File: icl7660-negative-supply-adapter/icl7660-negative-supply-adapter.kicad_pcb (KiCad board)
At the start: 2 copper layers, 33 x 45.7 mm, 11 parts, among them J1 Power Supply, J2 Eurorack_Power_Large, U1 ICL7660

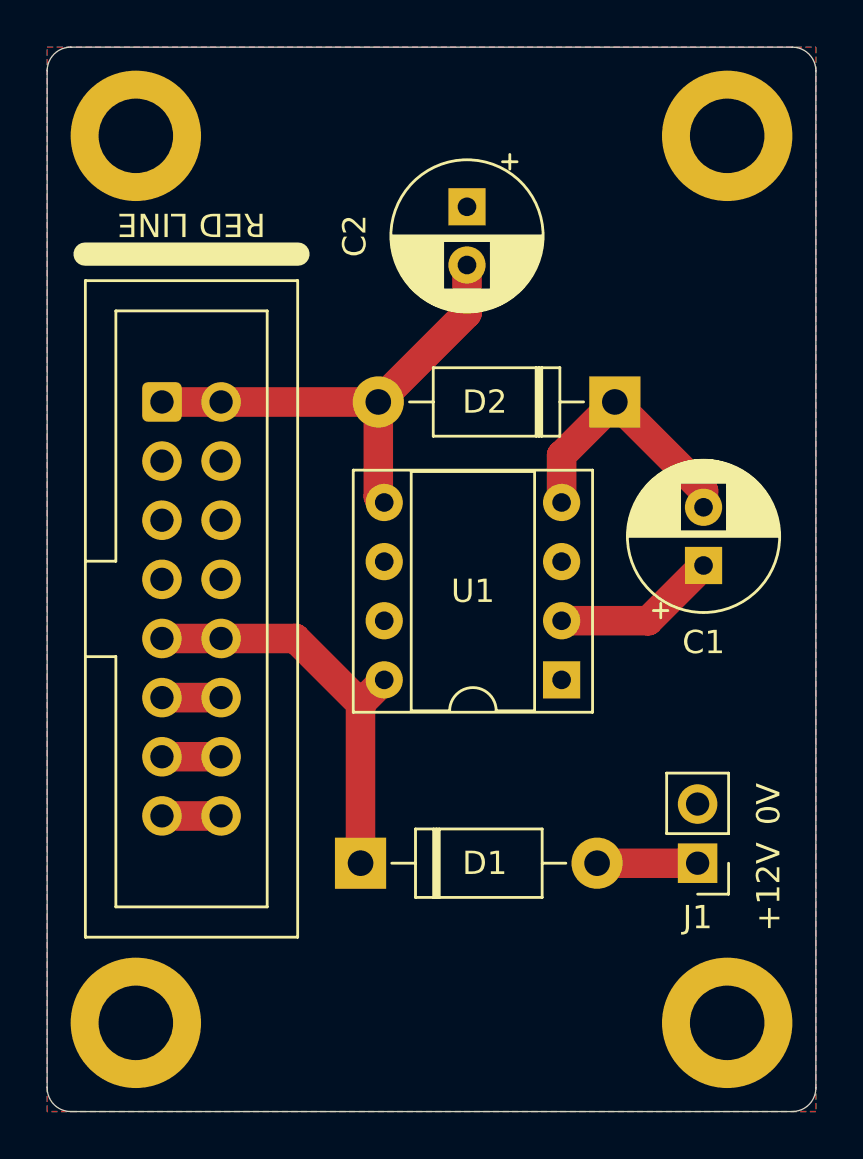
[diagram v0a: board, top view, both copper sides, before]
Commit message: update iclc7660 adapter with new footprints
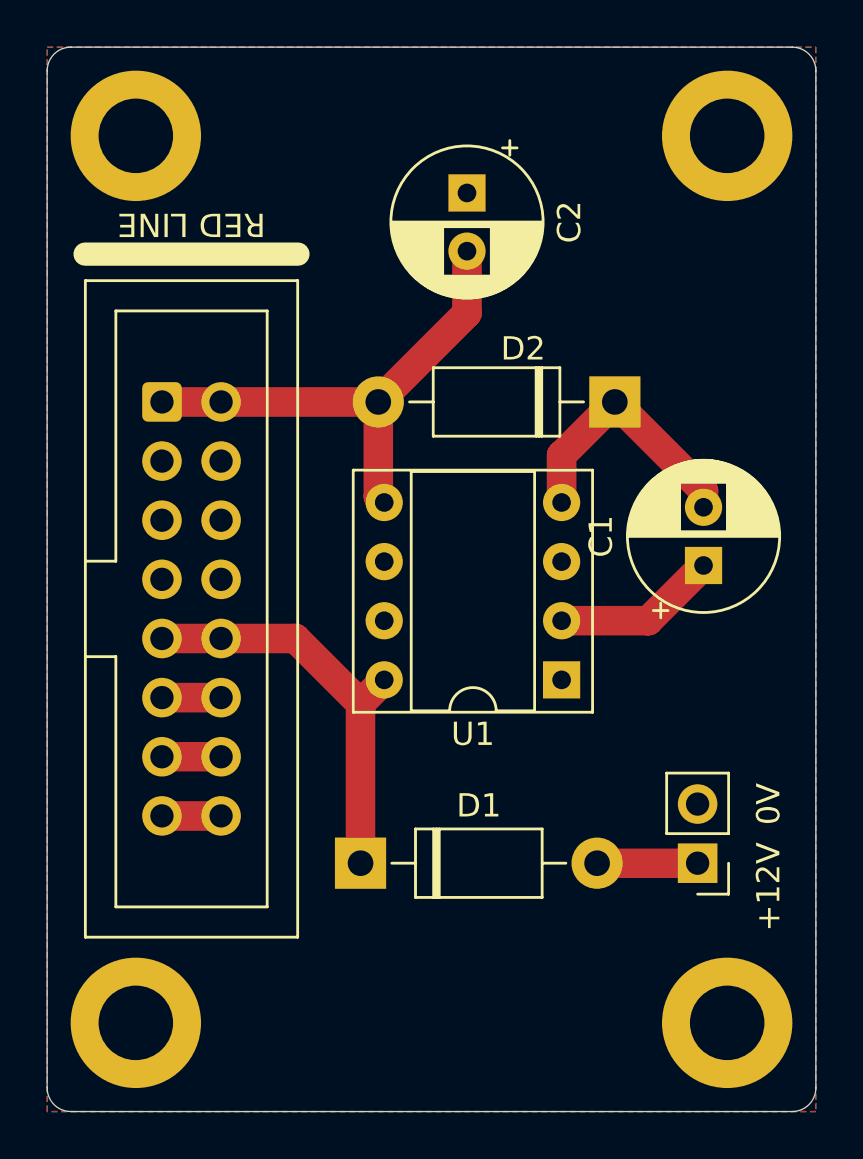
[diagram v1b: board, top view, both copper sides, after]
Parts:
- C1, C2: footprint Rumblesan_Footprints:CP_Radial_D6.3mm_P2.50mm -> rumblesan-standard-parts:CP_Radial_D6.3mm_P2.50mm
- D1, D2: footprint Rumblesan_Footprints:D_DO-41_SOD81_P10.16mm_Horizontal -> rumblesan-standard-parts:D_DO-41_SOD81_P10.16mm_Horizontal
- H1, H2, H3, H4: footprint MountingHole:MountingHole_3.2mm_M3_DIN965_Pad -> rumblesan-standard-parts:MountingHole_3.2mm_M3_DIN965_Pad
- J2: value Eurorack_Power_Large -> Eurorack_Bus_Power; footprint EurorackBasics:Eurorack_PowerHeader_2x08_P2.54mm_Shrouded -> eurorack-power:Eurorack_PowerHeader_2x08_P2.54mm_Shrouded
- U1: footprint Rumblesan_Footprints:DIP-8_W7.62mm_Socket -> rumblesan-standard-parts:DIP-8_W7.62mm_Socket
- moved C2 0.59 mm to (142.0, 84.5)
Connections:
- J2 pad 11: unconnected-(J2-Pad11) -> Net-(J2-Pad11)
- J2 pad 12: unconnected-(J2-Pad11) -> Net-(J2-Pad11)
- J2 pad 13: unconnected-(J2-Pad13) -> Net-(J2-Pad13)
- J2 pad 14: unconnected-(J2-Pad13) -> Net-(J2-Pad13)
- J2 pad 15: unconnected-(J2-Pad15) -> Net-(J2-Pad15)
- J2 pad 16: unconnected-(J2-Pad15) -> Net-(J2-Pad15)
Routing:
- net unconnected-(J2-Pad15): track 2.54 -> 0.00 mm
- net unconnected-(J2-Pad13): track 2.54 -> 0.00 mm
- net unconnected-(J2-Pad11): track 2.54 -> 0.00 mm
- net Net-(J2-Pad15): track 0.00 -> 2.54 mm
- net Net-(J2-Pad13): track 0.00 -> 2.54 mm
- net Net-(J2-Pad11): track 0.00 -> 2.54 mm
- net Net-(C2-Pad2): track 21.2 -> 21.8 mm

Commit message: Creating gerbers for negative supply adapter
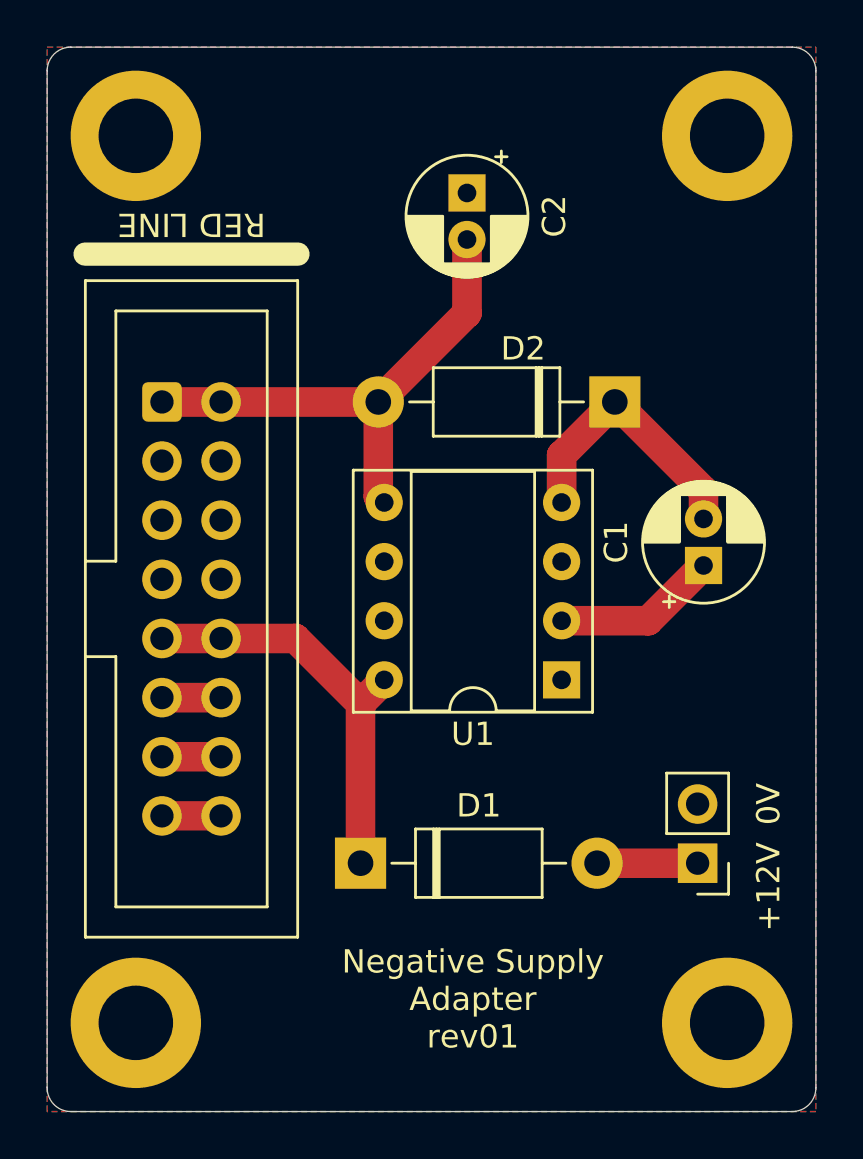
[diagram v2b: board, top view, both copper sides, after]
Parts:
- C1, C2: footprint rumblesan-standard-parts:CP_Radial_D6.3mm_P2.50mm -> rumblesan-standard-parts:CP_Radial_D5.0mm_P2.00mm
- J2: value Eurorack_Bus_Power -> Eurorack Bus Power
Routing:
- net Net-(C2-Pad2): track 21.8 -> 22.3 mm
- net Net-(C1-Pad2): track 11.4 -> 11.9 mm
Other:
- board text added: "Negative Supply Adapter rev01"
